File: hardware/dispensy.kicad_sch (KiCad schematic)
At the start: 0 parts

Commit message: work on pi schematic
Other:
- title: (none) -> Dispensy Mainboard
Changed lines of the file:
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@@
   (paper "A4")
   (title_block
+    (title "Dispensy Mainboard")
+    (date "2023-02-19")
     (company "DrinkRobotics")
+    (comment 2 "!! PCB Thickness: 1mm !!")
+    (comment 4 "DRAFT DRAFT DRAFT DRAFT DRAFT")
   )
   (sheet (at 66.04 54.61) (size 34.29 33.02) (fields_autoplaced)

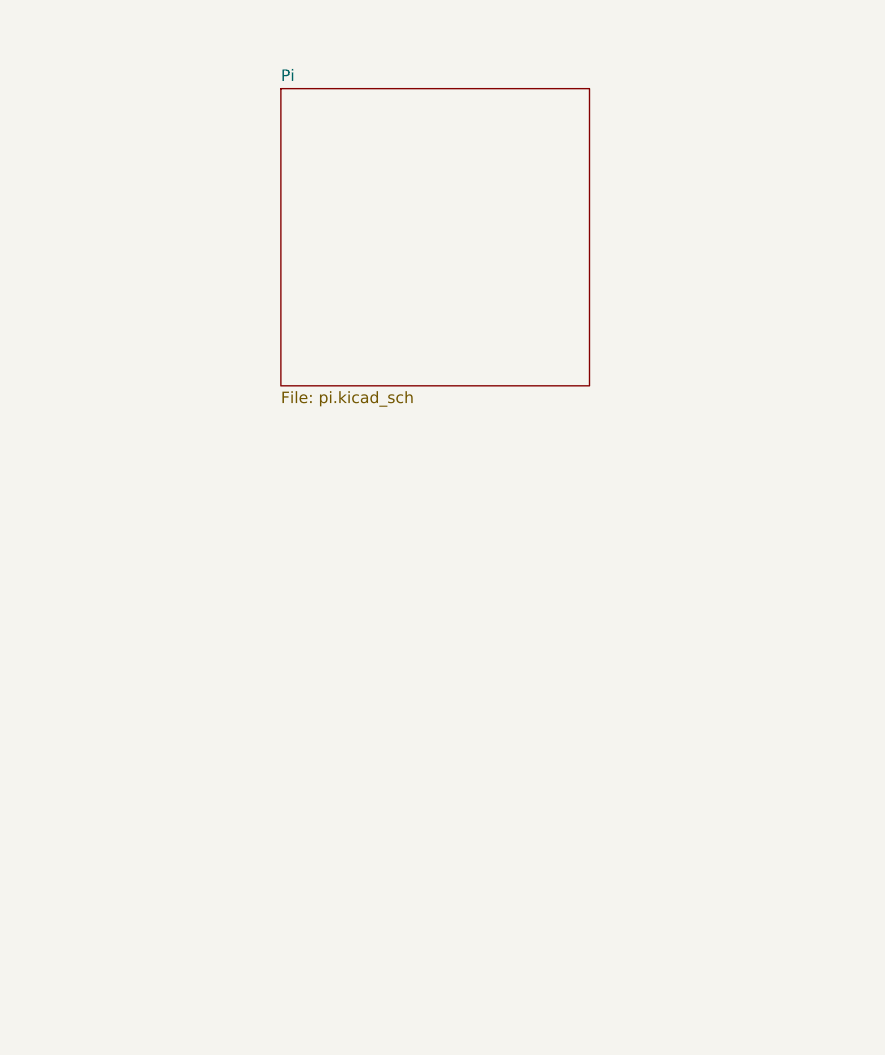
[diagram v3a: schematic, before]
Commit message: put lm2576 in own schematic sheet
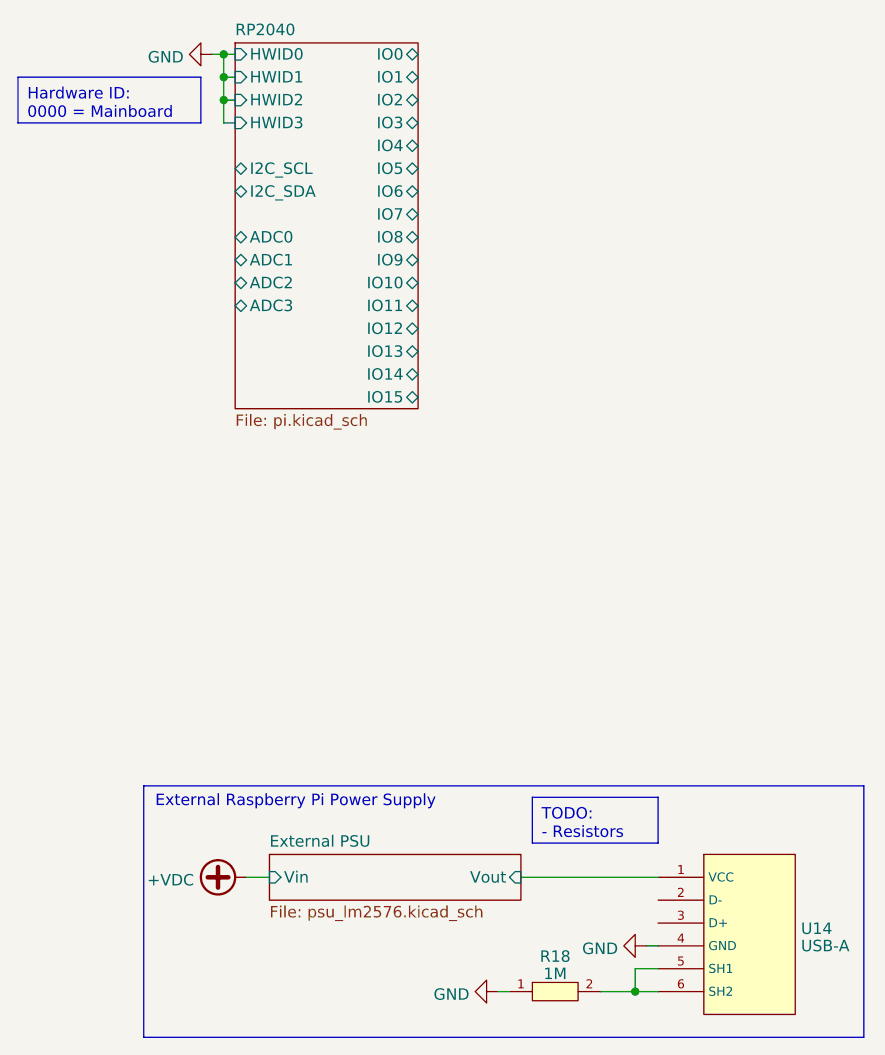
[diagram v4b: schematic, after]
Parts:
- added R18: 1M, jlc_footprints:R0402, symbol jlc:AC0402FR-071ML
- added U14: USB-A, jlc_footprints:USB-A-TH_USB-302-T, symbol jlc:U-USBAR04P-F000
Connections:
- new net: R18.2, U14.5 (SH1), U14.6 (SH2)
- new net External PSU/Vout: U14.1 (VCC)
- new net GND: R18.1, U14.4 (GND)
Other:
- sheet Pi renamed RP2040
- added sheet External PSU (psu_lm2576.kicad_sch)
- sheet RP2040 ports: added ADC0, ADC1, ADC2, ADC3, HWID0, HWID1, HWID2, HWID3, I2C_SCL, I2C_SDA, IO0, IO1, IO10, IO11, IO12, IO13, IO14, IO15, IO2, IO3, IO4, IO5, IO6, IO7, IO8, IO9; removed none
- note added: "External Raspberry Pi Power Supply"

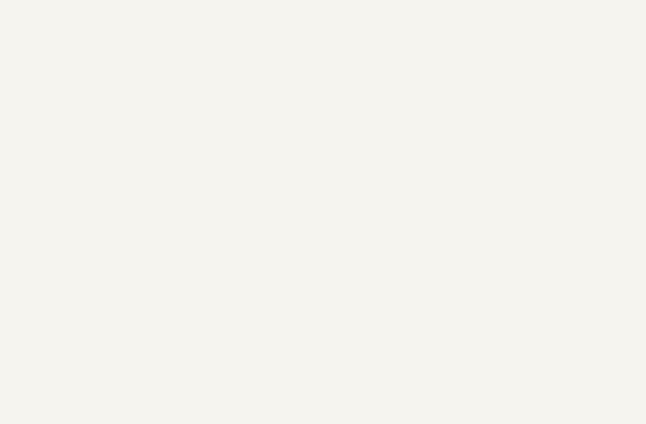
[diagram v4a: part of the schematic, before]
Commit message: add power connector on mainboard
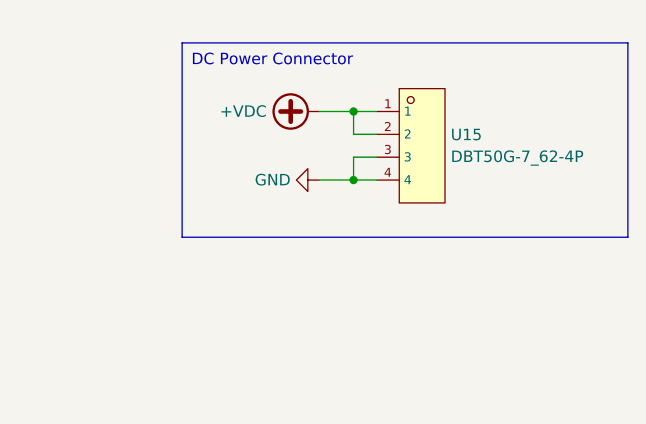
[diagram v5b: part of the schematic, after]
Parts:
- added U15: DBT50G-7_62-4P, jlc_footprints:CONN-TH_4P-P7.62_L15.2-W31.7-EX4.2, symbol jlc:DBT50G-7_62-4P
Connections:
- net +VDC: now also U15.1, U15.2
- net GND: now also U15.3, U15.4
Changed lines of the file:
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@@
   (title_block
     (title "Dispensy Mainboard")
-    (date "2023-02-20")
+    (date "2024-01-10")
     (rev "0")
     (company "DrinkRobotics")
@@
     (comment 4 "DRAFT DRAFT DRAFT DRAFT DRAFT")
   )
+  (junction (at 140.97 57.15) (diameter 0) (color 0 0 0 0)
+  )
+  (junction (at 140.97 64.77) (diameter 0) (color 0 0 0 0)
+  )
   (junction (at 105.41 154.94) (diameter 0) (color 0 0 0 0)
   )
@@
     (stroke (width 0) (type default))
   )
+  (wire (pts (xy 140.97 62.23) (xy 140.97 64.77))
+    (stroke (width 0) (type default))
+  )
+  (wire (pts (xy 143.51 62.23) (xy 140.97 62.23))
+    (stroke (width 0) (type default))
+  )
   (wire (pts (xy 106.68 149.86) (xy 107.95 149.86))
     (stroke (width 0) (type default))
@@
     (stroke (width 0) (type default))
   )
+  (wire (pts (xy 140.97 59.69) (xy 140.97 57.15))
+    (stroke (width 0) (type default))
+  )
+  (wire (pts (xy 137.16 64.77) (xy 140.97 64.77))
+    (stroke (width 0) (type default))
+  )
   (wire (pts (xy 90.17 154.94) (xy 91.44 154.94))
     (stroke (width 0) (type default))
   )
+  (wire (pts (xy 140.97 57.15) (xy 143.51 57.15))
+    (stroke (width 0) (type default))
+  )
   (wire (pts (xy 59.69 55.88) (xy 59.69 53.34))
     (stroke (width 0) (type default))
@@
     (stroke (width 0) (type default))
   )
+  (wire (pts (xy 137.16 57.15) (xy 140.97 57.15))
+    (stroke (width 0) (type default))
+  )
+  (wire (pts (xy 143.51 59.69) (xy 140.97 59.69))
+    (stroke (width 0) (type default))
+  )
   (wire (pts (xy 59.69 53.34) (xy 59.69 50.8))
     (stroke (width 0) (type default))
   )
   (wire (pts (xy 92.71 142.24) (xy 107.95 142.24))
+    (stroke (width 0) (type default))
+  )
+  (wire (pts (xy 140.97 64.77) (xy 143.51 64.77))
     (stroke (width 0) (type default))
   )
@@
   (text_box "Hardware ID:\n0000 = Mainboard"
     (at 36.83 53.34 0) (size 20.32 5.08)
+    (stroke (width 0) (type default))
+    (fill (type none))
+    (effects (font (size 1.27 1.27)) (justify left top))
+  )
+  (text_box "DC Power Connector"
+    (at 121.92 49.53 0) (size 49.53 21.59)
     (stroke (width 0) (type default))
     (fill (type none))
@@
     )
   )
+  (symbol (lib_id "power:+VDC") (at 137.16 57.15 90) (unit 1)
+    (in_bom yes) (on_board yes) (dnp no) (fields_autoplaced)
+    (property "Reference" "#PWR054" (at 139.7 57.15 0)
+      (effects (font (size 1.27 1.27)) hide)
+    )
+    (property "Value" "+VDC" (at 131.318 57.15 90)
+      (effects (font (size 1.27 1.27)) (justify left))
+    )
+    (property "Footprint" "" (at 137.16 57.15 0)
+      (effects (font (size 1.27 1.27)) hide)
+    )
+    (property "Datasheet" "" (at 137.16 57.15 0)
+      (effects (font (size 1.27 1.27)) hide)
+    )
+    (pin "1")
+    (instances
+      (project "dispensy"
+        (path "/a50b51f9-900f-4bbb-8934-4acbc429c37b"
+          (reference "#PWR054") (unit 1)
+        )
+      )
+    )
+  )
+  (symbol (lib_id "jlc:DBT50G-7_62-4P") (at 148.59 60.96 0) (unit 1)
+    (in_bom yes) (on_board yes) (dnp no) (fields_autoplaced)
+    (property "Reference" "U15" (at 151.765 59.7479 0)
+      (effects (font (size 1.27 1.27)) (justify left))
+    )
+    (property "Value" "DBT50G-7_62-4P" (at 151.765 62.1721 0)
+      (effects (font (size 1.27 1.27)) (justify left))
+    )
+    (property "Footprint" "jlc_footprints:CONN-TH_4P-P7.62_L15.2-W31.7-EX4.2" (at 148.59 71.12 0)
+      (effects (font (size 1.27 1.27) italic) hide)
+    )
+    (property "Datasheet" "https://item.szlcsc.com/512151.html?ref=editor&logined=true" (at 146.304 60.833 0)
+      (effects (font (size 1.27 1.27)) (justify left) hide)
+    )
+    (property "LCSC" "C496132" (at 148.59 60.96 0)
+      (effects (font (size 1.27 1.27)) hide)
+    )
+    (pin "4")
+    (pin "3")
+    (pin "1")
+    (pin "2")
+    (instances
+      (project "dispensy"
+        (path "/a50b51f9-900f-4bbb-8934-4acbc429c37b"
+          (reference "U15") (unit 1)
+        )
+      )
+    )
+  )
   (symbol (lib_id "jlc:AC0402FR-071ML") (at 96.52 154.94 0) (unit 1)
     (in_bom yes) (on_board yes) (dnp no) (fields_autoplaced)
@@
         )
       )
+    )
+  )
+  (symbol (lib_id "power:GND") (at 137.16 64.77 270) (unit 1)
+    (in_bom yes) (on_board yes) (dnp no) (fields_autoplaced)
+    (property "Reference" "#PWR055" (at 130.81 64.77 0)
+      (effects (font (size 1.27 1.27)) hide)
+    )
+    (property "Value" "GND" (at 133.9851 64.77 90)
+      (effects (font (size 1.27 1.27)) (justify right))
+    )
+    (property "Footprint" "" (at 137.16 64.77 0)
+      (effects (font (size 1.27 1.27)) hide)
+    )
+    (property "Datasheet" "" (at 137.16 64.77 0)
+      (effects (font (size 1.27 1.27)) hide)
+    )
+    (pin "1")
+    (instances
+      (project "dispensy"
+        (path "/a50b51f9-900f-4bbb-8934-4acbc429c37b"
+          (reference "#PWR055") (unit 1)
+        )
+      )

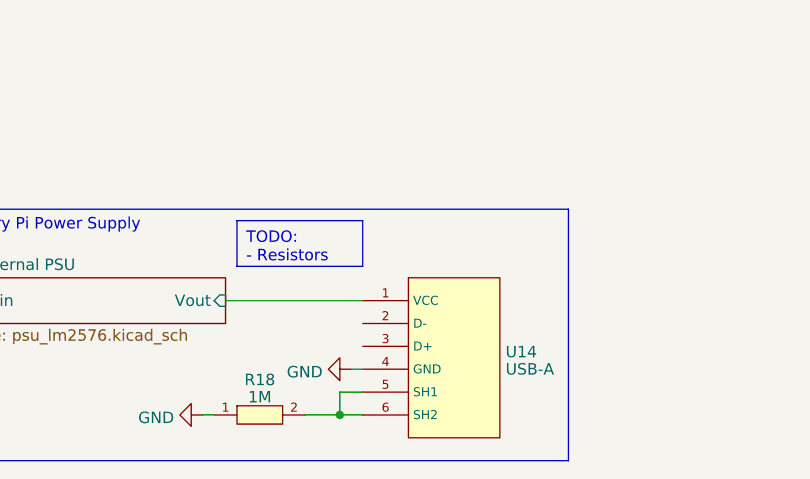
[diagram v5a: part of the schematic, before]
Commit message: short data lines on usb-a for powering external device
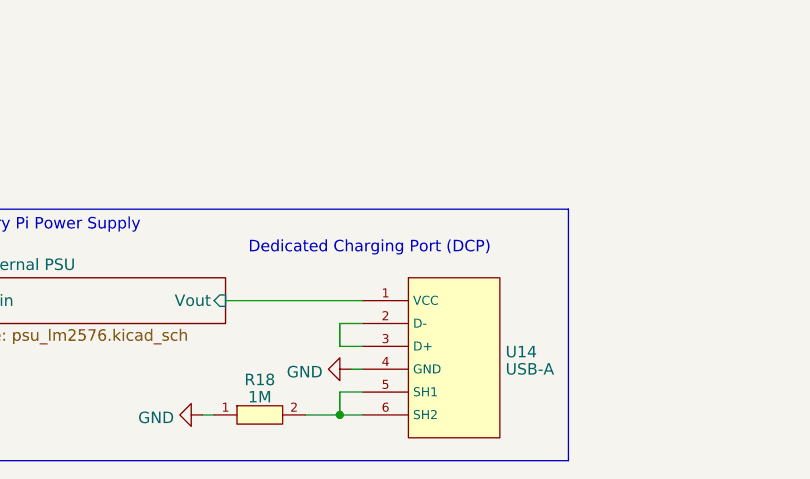
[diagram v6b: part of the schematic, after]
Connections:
- net at U14.2 (D-): now also U14.3 (D+)
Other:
- note added: "Dedicated Charging Port (DCP)"
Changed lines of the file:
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@@
+    (stroke (width 0) (type default))
+  )
+  (wire (pts (xy 105.41 144.78) (xy 107.95 144.78))
     (stroke (width 0) (type default))
   )
@@
   )
   (wire (pts (xy 140.97 57.15) (xy 143.51 57.15))
+    (stroke (width 0) (type default))
+  )
+  (wire (pts (xy 107.95 147.32) (xy 105.41 147.32))
     (stroke (width 0) (type default))
   )
@@
     (stroke (width 0) (type default))
   )
+  (wire (pts (xy 105.41 147.32) (xy 105.41 144.78))
+    (stroke (width 0) (type default))
+  )
   (rectangle (start 50.8 132.08) (end 130.81 160.02)
     (stroke (width 0) (type default))
@@
     (effects (font (size 1.27 1.27)) (justify left top))
   )
-  (text_box "TODO:\n- Resistors"
-    (at 93.98 133.35 0) (size 13.97 5.08)
-    (stroke (width 0) (type default))
-    (fill (type none))
-    (effects (font (size 1.27 1.27)) (justify left top))
+  (text "Dedicated Charging Port (DCP)" (at 95.25 137.16 0)
+    (effects (font (size 1.27 1.27)) (justify left bottom) (href "https://electronics.stackexchange.com/a/200581"))
   )
   (text "External Raspberry Pi Power Supply" (at 52.07 134.62 0)
